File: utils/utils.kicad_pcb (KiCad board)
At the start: 2 copper layers, 34.8 x 70.5 mm, 37 parts, among them J1 A_IN, J2 B_IN, J3 GATE, J4 EURORACK_CONN_10, J5 ~OUT, J6 OUT, J7 Conn_01x04, J8 Conn_01x05, J9 Conn_01x03_Male, Q1 2N3904, U1 TL072, U2 4066, U3 LM317L_TO92, U4 LM337L_TO92

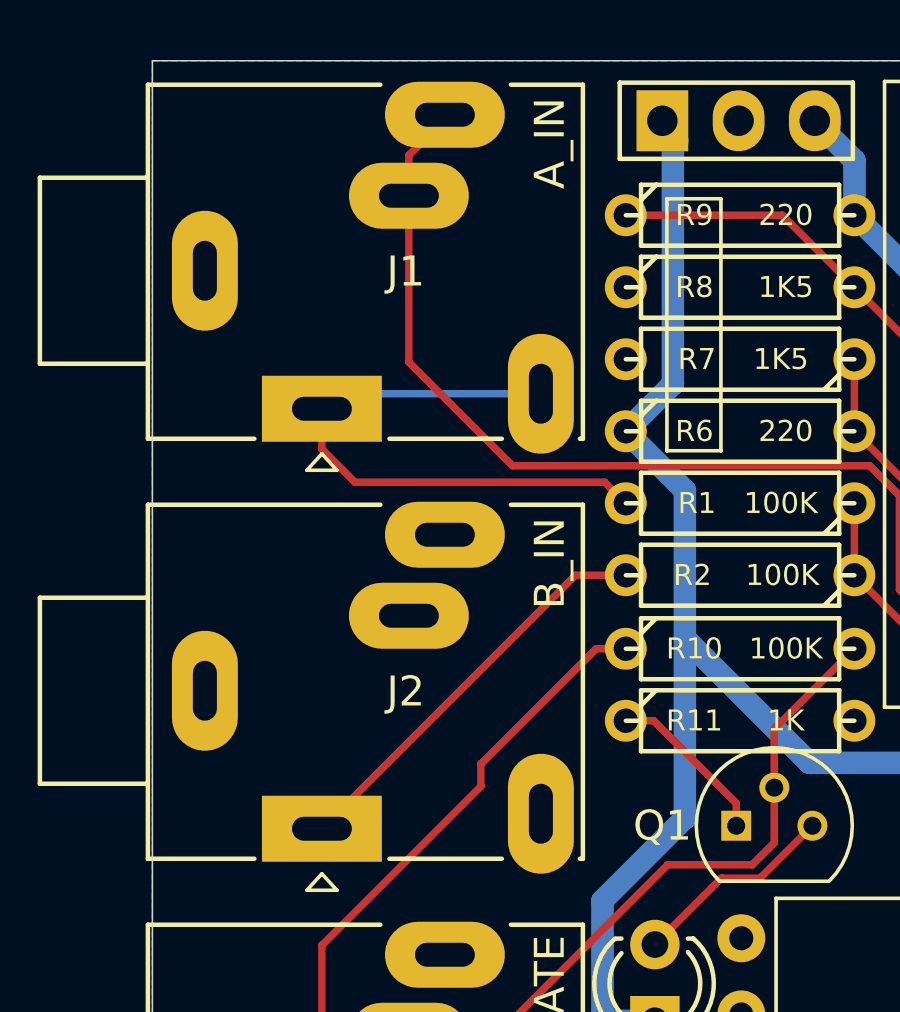
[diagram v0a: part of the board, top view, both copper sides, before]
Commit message: correct ground issue
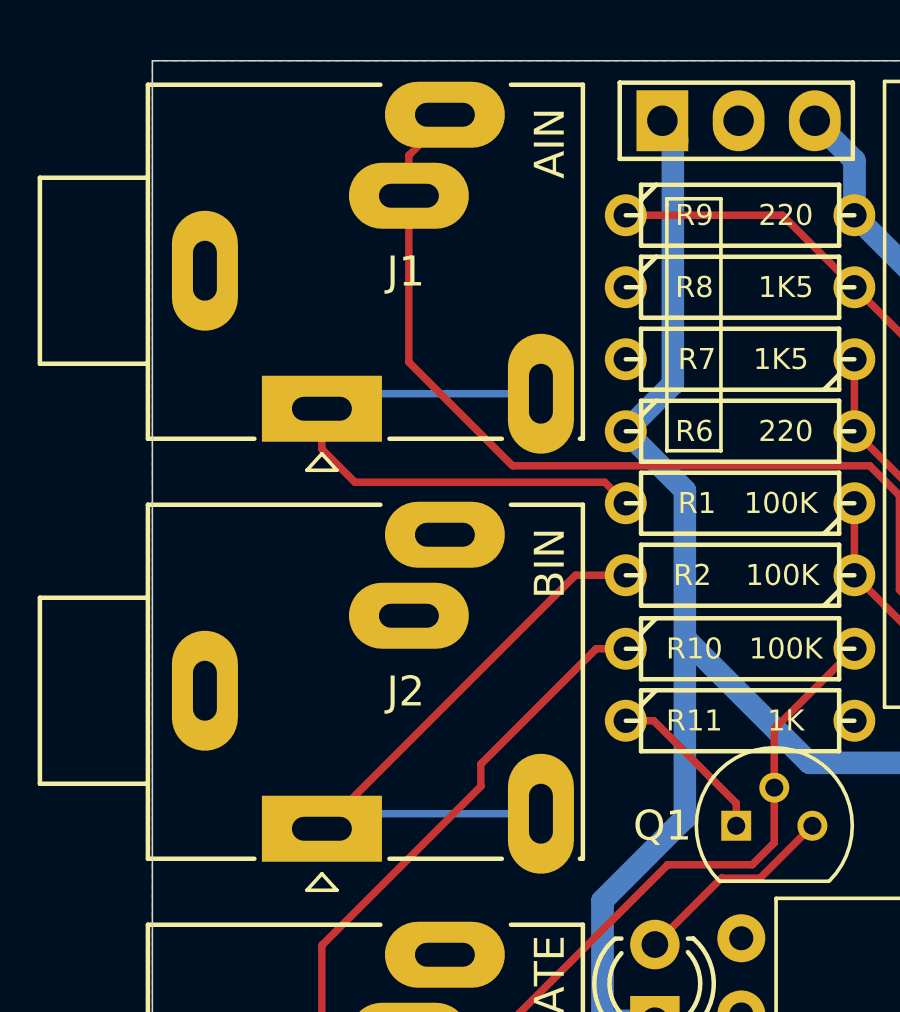
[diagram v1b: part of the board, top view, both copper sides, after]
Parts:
- J1: value A_IN -> AIN
- J2: value B_IN -> BIN
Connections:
- J2 pad TN: GND -> BIN
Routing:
- net BIN: track 13.6 -> 21.1 mm
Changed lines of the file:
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@@
     (thickness 1.6)
     (drawings 14)
-    (tracks 269)
+    (tracks 271)
     (zones 0)
     (modules 37)
@@
       (effects (font (size 1 1) (thickness 0.15)))
     )
-    (fp_text value A_IN (at 7.6 -8.85 90) (layer F.SilkS)
+    (fp_text value AIN (at 7.6 -8.85 90) (layer F.SilkS)
       (effects (font (size 1 1) (thickness 0.15)))
     )
@@
       (effects (font (size 1 1) (thickness 0.15)))
     )
-    (fp_text value B_IN (at 7.6 -8.85 270) (layer F.SilkS)
+    (fp_text value BIN (at 7.6 -8.85 270) (layer F.SilkS)
       (effects (font (size 1 1) (thickness 0.15)))
     )
@@
       (net 3 BIN))
     (pad TN thru_hole oval (at 7.3 -0.5 90) (size 4 2.2) (drill oval 2 0.8) (layers *.Cu *.Mask)
-      (net 1 GND))
+      (net 3 BIN))
     (pad SN thru_hole oval (at 2.9 -7.1) (size 4 2.2) (drill oval 2 0.8) (layers *.Cu *.Mask)
       (net 1 GND))
@@
   (segment (start 137.35 60.15) (end 128.9 68.6) (width 0.25) (layer F.Cu) (net 3))
   (segment (start 139.03 60.15) (end 137.35 60.15) (width 0.25) (layer F.Cu) (net 3))
+  (segment (start 129.4 68.1) (end 128.9 68.6) (width 0.25) (layer B.Cu) (net 3))
+  (segment (start 136.2 68.1) (end 129.4 68.1) (width 0.25) (layer B.Cu) (net 3))
   (segment (start 151.516 98.1) (end 151.192 98.424) (width 0.25) (layer F.Cu) (net 4))
   (segment (start 154.5 98.1) (end 151.516 98.1) (width 0.25) (layer F.Cu) (net 4))

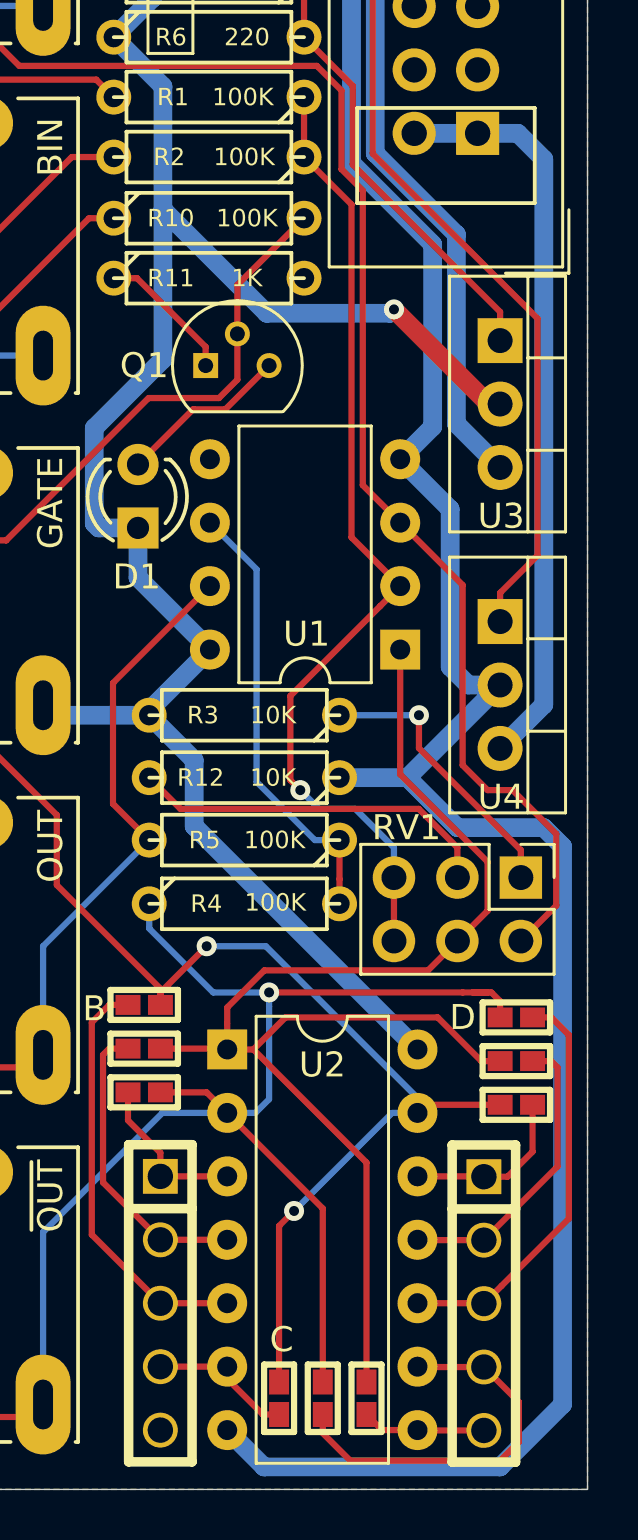
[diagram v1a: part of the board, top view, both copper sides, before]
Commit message: fix some bugs in the circuit
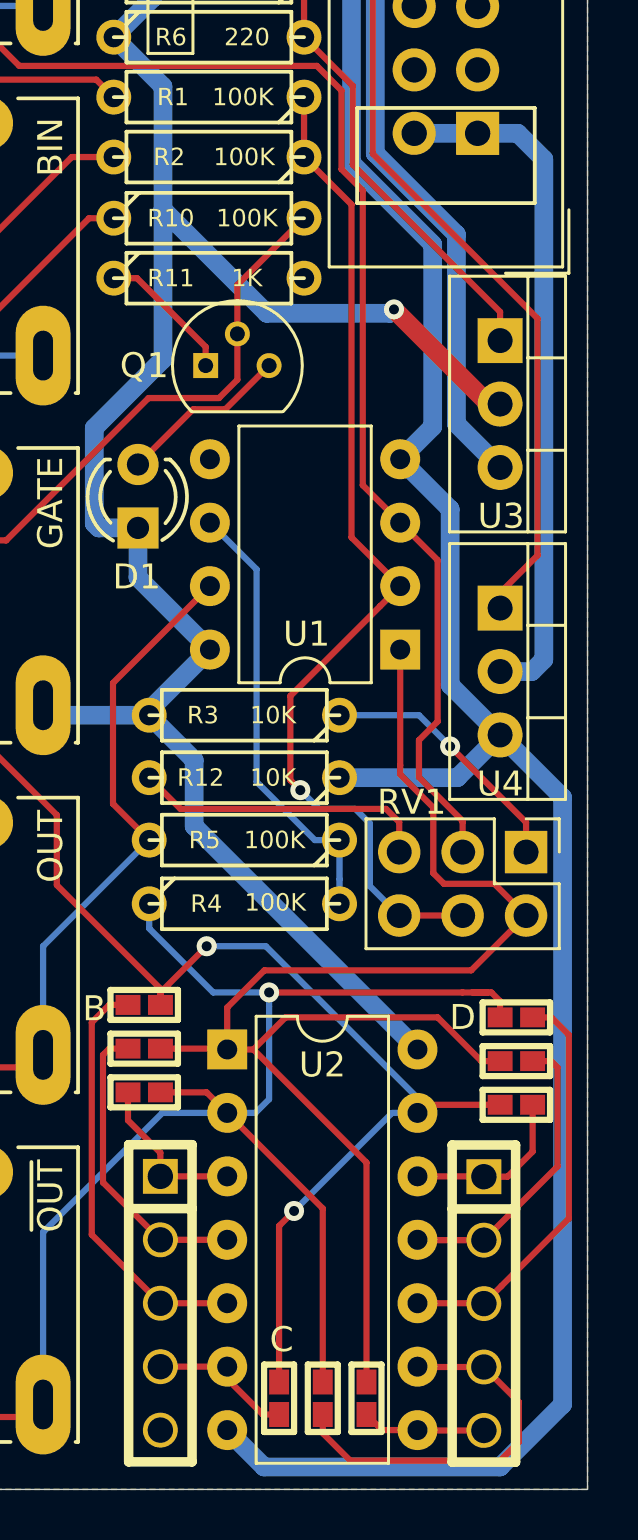
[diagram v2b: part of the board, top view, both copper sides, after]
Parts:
- U3: value LM317L_TO92 -> LM317
- U4: value LM337L_TO92 -> LM337
- moved RV1 1.04 mm to (153.0, 89.2)
- moved U4 0.54 mm to (154.5, 78.2)
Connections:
- U4 pad 2: -10V -> Net-(J4-Pad1)
- U4 pad 3: Net-(J4-Pad1) -> -10V
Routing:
- net A_CONN: track 65.7 -> 60.1 mm
- net STAGE1_OUT: track 55.7 -> 59.2 mm
- net Net-(R12-Pad2): track 14.7 -> 11.9 mm
- net Net-(J4-Pad1): track 29.9 -> 27.6 mm
- net -10V: track 95.2 -> 93.2 mm
- net Net-(R1-Pad1): track 40.0 -> 41.4 mm
- net Net-(R3-Pad1): track 11.4 -> 10.4 mm

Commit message: reworked utilities around better analog switch modules
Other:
- board text added: "TODO: this connector is backwards"

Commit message: restarted pcb
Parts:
- removed J1: AIN, synth:Jack_3.5mm_Ledino_KB3SPRS_Horizontal
- removed J2: BIN, synth:Jack_3.5mm_Ledino_KB3SPRS_Horizontal
- removed J3: GATE, synth:Jack_3.5mm_Ledino_KB3SPRS_Horizontal
- removed J4: EURORACK_CONN_10, synth:EURORACK_10_IDC
- removed J5: ~OUT, synth:Jack_3.5mm_Ledino_KB3SPRS_Horizontal
- removed J7: Conn_01x04, imciner2/KiCad-Libraries/modules/Connectors.pretty:CONN_2.54mm_1x05
- removed J8: Conn_01x05, imciner2/KiCad-Libraries/modules/Connectors.pretty:CONN_2.54mm_1x05
- removed J9: Conn_01x03_Male, 4ms/4ms-kicad-lib/4ms-footprints.pretty:Pin_Header_Straight_1x03
- removed JP1, JP2, JP3, JP4, JP5, JP6, JP7, JP8, JP9: Jumper_2_Open, fruchti/fruchtilib/mod/rcl.pretty:SOLDER_JUMPER_0603_B
- removed R10: 100K, 4ms/4ms-kicad-lib/4ms-footprints.pretty:Resistor_TH_300
- removed R11: 1K, 4ms/4ms-kicad-lib/4ms-footprints.pretty:Resistor_TH_300
- removed R12: 10K, 4ms/4ms-kicad-lib/4ms-footprints.pretty:Resistor_TH_300
- removed U3: LM317, KiCad/TO_SOT_Packages_THT.pretty:TO-220-3_Vertical
- removed U4: LM337, KiCad/TO_SOT_Packages_THT.pretty:TO-220-3_Vertical
- added A_IN1: AudioJack2_Ground_Switch, synth:Jack_3.5mm_Ledino_KB3SPRS_Horizontal, F.Cu at (125.5, 50.0)
- added B_IN1: AudioJack2_Ground_Switch, synth:Jack_3.5mm_Ledino_KB3SPRS_Horizontal, F.Cu at (125.5, 64.0)
- added GATE1: AudioJack2_Ground_Switch, synth:Jack_3.5mm_Ledino_KB3SPRS_Horizontal, F.Cu at (125.5, 78.0)
- added OUT1: AudioJack2_Ground_Switch, synth:Jack_3.5mm_Ledino_KB3SPRS_Horizontal, F.Cu at (125.5, 92.0)
- added Q2: 2N3904, Package_TO_SOT_THT:TO-92, F.Cu at (141.5, 53.5)
- added Q3: 2N3904, Package_TO_SOT_THT:TO-92, F.Cu at (141.0, 61.0)
- added ~OUT1: AudioJack2_Ground_Switch, synth:Jack_3.5mm_Ledino_KB3SPRS_Horizontal, F.Cu at (125.5, 106.0)
- J6: value OUT -> EURORACK_CONN_16; footprint synth:Jack_3.5mm_Ledino_KB3SPRS_Horizontal -> synth:EURORACK_16_IDC
- Q1: footprint 4ms/4ms-kicad-lib/lib-footprints/4ms_Package_TO.pretty:TO-92_OffsetPin2 -> Package_TO_SOT_THT:TO-92
- R1, R2, R4, R5: footprint 4ms/4ms-kicad-lib/4ms-footprints.pretty:Resistor_TH_300 -> Resistor_THT:R_Axial_DIN0309_L9.0mm_D3.2mm_P2.54mm_Vertical
- R3: value 10K -> 100K; footprint 4ms/4ms-kicad-lib/4ms-footprints.pretty:Resistor_TH_300 -> Resistor_THT:R_Axial_DIN0309_L9.0mm_D3.2mm_P2.54mm_Vertical
- R6, R9: value 220 -> 100K; footprint 4ms/4ms-kicad-lib/4ms-footprints.pretty:Resistor_TH_300 -> Resistor_THT:R_Axial_DIN0309_L9.0mm_D3.2mm_P2.54mm_Vertical
- R7: value 1K5 -> 100K; footprint 4ms/4ms-kicad-lib/4ms-footprints.pretty:Resistor_TH_300 -> Resistor_THT:R_Axial_DIN0309_L9.0mm_D3.2mm_P2.54mm_Vertical
- R8: value 1K5 -> 1K; footprint 4ms/4ms-kicad-lib/4ms-footprints.pretty:Resistor_TH_300 -> Resistor_THT:R_Axial_DIN0309_L9.0mm_D3.2mm_P2.54mm_Vertical
- RV1: footprint 4ms/4ms-kicad-lib/4ms-footprints.pretty:Pin_Header_Straight_2x03_Pitch2.54mm -> Connector_PinHeader_2.54mm:PinHeader_2x03_P2.54mm_Vertical
- U1: value TL072 -> TL074; footprint KiCad/kicad-footprints/Package_DIP.pretty:DIP-8_W7.62mm -> Package_DIP:DIP-14_W7.62mm
- U2: value 4066 -> DG403; footprint KiCad/kicad-footprints/Package_DIP.pretty:DIP-14_W7.62mm -> Package_SO:SOIC-16_3.9x9.9mm_P1.27mm
- moved R6 54.4 mm to (170.8, 102.0)
- moved R9 51.5 mm to (166.2, 94.0)
- moved J6 39.5 mm to (154.3, 66.3), turned to 180 degrees
- moved R5 36.0 mm to (146.0, 51.5), turned to 270 degrees
- moved U1 31.4 mm to (151.5, 111.2)
- moved R4 23.1 mm to (141.0, 67.2), turned to 270 degrees
- moved Q1 21.4 mm to (141.5, 47.2), turned to 90 degrees
- moved R3 19.4 mm to (146.2, 63.2), turned to 90 degrees
- moved R1 17.8 mm to (145.8, 75.3), turned to 90 degrees
- moved R7 16.6 mm to (146.0, 69.3), turned to 90 degrees
- moved R2 15.2 mm to (146.0, 45.2), turned to 270 degrees
- moved U2 7.88 mm to (143.5, 88.0)
- moved R8 7.03 mm to (140.7, 57.2)
- moved RV1 2.37 mm to (155.2, 90.0), turned to 180 degrees
- moved D1 0.90 mm to (140.8, 74.2)
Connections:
- D1 pad 2: +10V -> +5V
- Q1 pad 1: Net-(Q1-Pad1) -> GND
- Q1 pad 2: GATE_CONN -> A_CONN
- Q1 pad 3: Net-(D1-Pad1) -> CONST
- R1 pad 1: Net-(R1-Pad1) -> +5V
- R1 pad 2: AIN -> A_CONN
- R2 pad 1: Net-(R1-Pad1) -> +5V
- R2 pad 2: BIN -> CONST
- R3 pad 2: +10V -> AIN
- R4 pad 1: ~OUT -> Net-(R3-Pad1)
- R4 pad 2: Net-(R4-Pad2) -> BIN
- R5 pad 1: Net-(R4-Pad2) -> +5V
- R5 pad 2: OUT -> B_CONN
- R6 pad 1: +10V -> Net-(R6-Pad1)
- R7 pad 1: Net-(R6-Pad2) -> GATE
- R7 pad 2: GND -> GATE_CONN
- R8 pad 1: GND -> Net-(Q3-Pad1)
- R8 pad 2: Net-(R8-Pad2) -> GND
- R9 pad 1: Net-(R8-Pad2) -> Net-(R6-Pad2)
- R9 pad 2: -10V -> OUT
- RV1 pad 1: Net-(R3-Pad1) -> +12V
- RV1 pad 2: A_CONN -> Net-(RV1-Pad2)
- RV1 pad 3: Net-(R12-Pad2) -> -12V
- RV1 pad 4: STAGE1_OUT -> Net-(RV1-Pad4)
- RV1 pad 5: Net-(R1-Pad1) -> Net-(R3-Pad1)
- RV1 pad 6: Net-(R1-Pad1) -> Net-(R3-Pad1)
- U1 pad 1: STAGE1_OUT -> Net-(U1-Pad1)
- U1 pad 2: Net-(R1-Pad1) -> Net-(U1-Pad1)
- U1 pad 3: A_CONN -> Net-(RV1-Pad2)
- U1 pad 4: -10V -> +12V
- U1 pad 6: Net-(R4-Pad2) -> Net-(R3-Pad1)
- U1 pad 7: OUT -> Net-(RV1-Pad4)
- U1 pad 8: +10V -> OUT
- U2 pad 1: STAGE1_OUT -> Net-(U1-Pad1)
- U2 pad 10: 4066_10 -> GATE
- U2 pad 11: 4066_11 -> +12V
- U2 pad 12: 4066_12 -> +5V
- U2 pad 13: GATE -> GND
- U2 pad 14: +10V -> -12V
- U2 pad 2: ~OUT -> Net-(U2-Pad2)
- U2 pad 3: 4066_3 -> Net-(RV1-Pad4)
- U2 pad 4: 4066_4 -> Net-(U2-Pad16)
- U2 pad 5: 4066_5 -> Net-(R6-Pad1)
- U2 pad 6: 4066_6 -> GND
- U2 pad 7: -10V -> Net-(U2-Pad7)
- U2 pad 8: 4066_8 -> Net-(U2-Pad16)
- U2 pad 9: 4066_9 -> Net-(R6-Pad1)
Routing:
- net -10V: track 93.2 -> 0.00 mm
- net +10V: track 84.8 -> 0.00 mm, vias 1 -> 0
- net GATE: track 74.8 -> 0.00 mm, vias 2 -> 0
- net ~OUT: track 62.8 -> 0.00 mm, vias 1 -> 0
- net A_CONN: track 60.1 -> 0.00 mm
- net STAGE1_OUT: track 59.2 -> 0.00 mm
- net Net-(R1-Pad1): track 41.4 -> 0.00 mm, vias 1 -> 0
- net Net-(R8-Pad2): track 41.3 -> 0.00 mm
- net OUT: track 30.2 -> 0.00 mm
- net Net-(J4-Pad9): track 28.8 -> 0.00 mm
- net Net-(J4-Pad1): track 27.6 -> 0.00 mm
- net GATE_CONN: track 22.4 -> 0.00 mm
- net BIN: track 21.1 -> 0.00 mm
- net AIN: track 19.7 -> 0.00 mm
- net Net-(R4-Pad2): track 18.0 -> 0.00 mm
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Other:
- board text removed: "B"
- board text removed: "C"
- board text removed: "D"
- board text removed: "TODO: this connector is backwards"

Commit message: rework PCB
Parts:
- R1, R3, R8: footprint Resistor_THT:R_Axial_DIN0309_L9.0mm_D3.2mm_P2.54mm_Vertical -> Resistor_THT:R_Axial_DIN0204_L3.6mm_D1.6mm_P5.08mm_Horizontal
- moved R6 29.7 mm to (141.2, 98.3), turned to 90 degrees
- moved R9 25.1 mm to (141.2, 92.3), turned to 90 degrees
- moved R1 18.0 mm to (146.0, 57.2), turned to 180 degrees
- moved RV1 16.1 mm to (152.2, 74.2), turned to 0 degrees
- moved R8 8.00 mm to (146.0, 63.2), turned to 180 degrees
- moved Q3 7.18 mm to (145.2, 66.8)
- moved U1 6.02 mm to (153.1, 105.5)
- moved R7 5.47 mm to (145.8, 74.8)
- moved U2 4.50 mm to (144.0, 83.5), turned to 90 degrees
- moved R3 3.00 mm to (146.1, 60.2), turned to 180 degrees
- moved R4 0.52 mm to (140.8, 66.8)
- moved D1 0.50 mm to (140.8, 73.7)
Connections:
- U2 pad 1: Net-(U1-Pad1) -> Net-(U2-Pad1)
- U2 pad 10: GATE -> CONST
- U2 pad 15: CONST -> GATE
- U2 pad 16: Net-(U2-Pad16) -> Net-(R6-Pad1)
- U2 pad 3: Net-(RV1-Pad4) -> GND
- U2 pad 4: Net-(U2-Pad16) -> Net-(R6-Pad1)
- U2 pad 5: Net-(R6-Pad1) -> Net-(U2-Pad1)
- U2 pad 6: GND -> Net-(RV1-Pad4)
- U2 pad 8: Net-(U2-Pad16) -> Net-(U1-Pad1)
- U2 pad 9: Net-(R6-Pad1) -> Net-(U2-Pad1)
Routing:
- net +12V: track 0.00 -> 70.4 mm, vias 0 -> 1
- net +5V: track 0.00 -> 64.3 mm, vias 0 -> 1
- net -12V: track 0.00 -> 50.6 mm, vias 0 -> 1
- net Net-(R3-Pad1): track 0.00 -> 48.1 mm, vias 0 -> 1
- net CONST: track 0.00 -> 45.4 mm
- net Net-(R6-Pad1): track 0.00 -> 31.3 mm
- net Net-(RV1-Pad2): track 0.00 -> 28.7 mm
- net Net-(RV1-Pad4): track 0.00 -> 27.1 mm, vias 0 -> 1
- net GATE: track 0.00 -> 24.1 mm
- net A_CONN: track 0.00 -> 23.2 mm
- net ~OUT: track 0.00 -> 21.9 mm
- net Net-(U1-Pad1): track 0.00 -> 21.4 mm
- net GATE_CONN: track 0.00 -> 20.7 mm
- net OUT: track 0.00 -> 20.5 mm
- net B_CONN: track 0.00 -> 20.3 mm
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
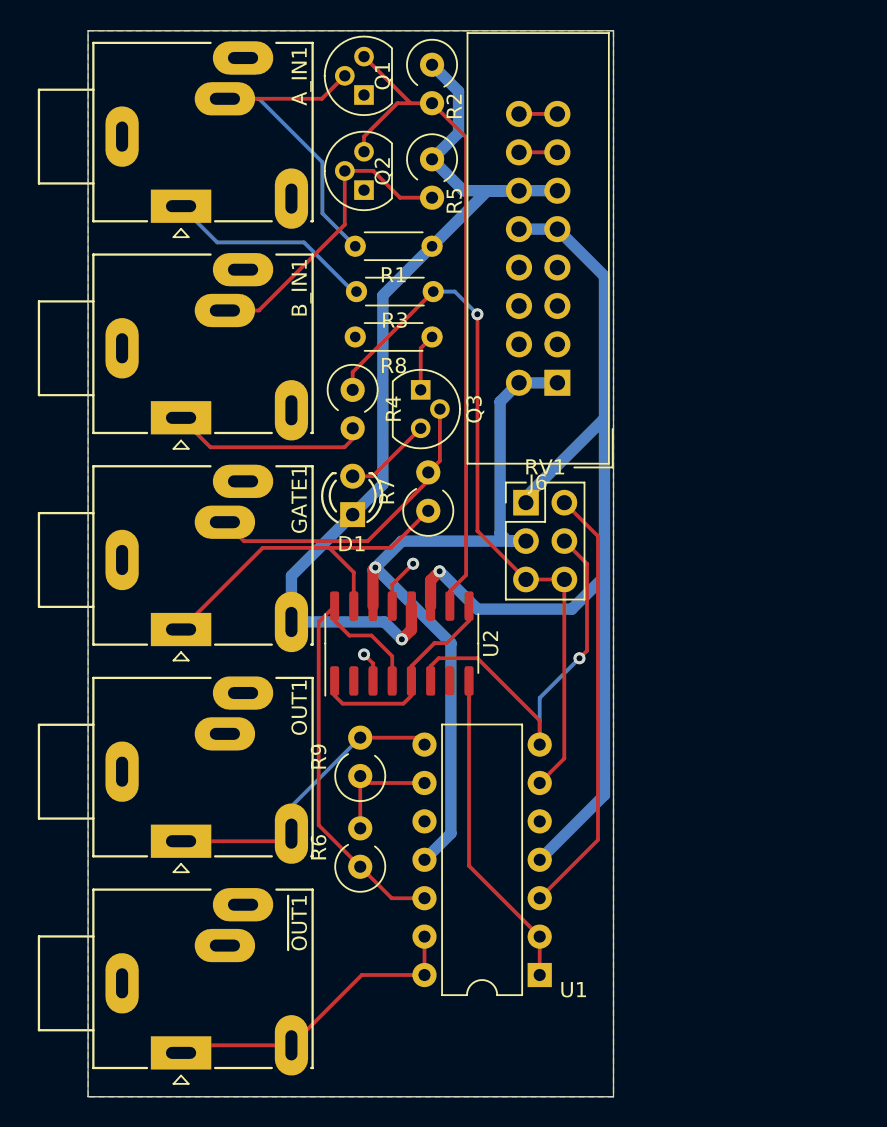
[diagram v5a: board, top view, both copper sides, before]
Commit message: reworked silkscreen
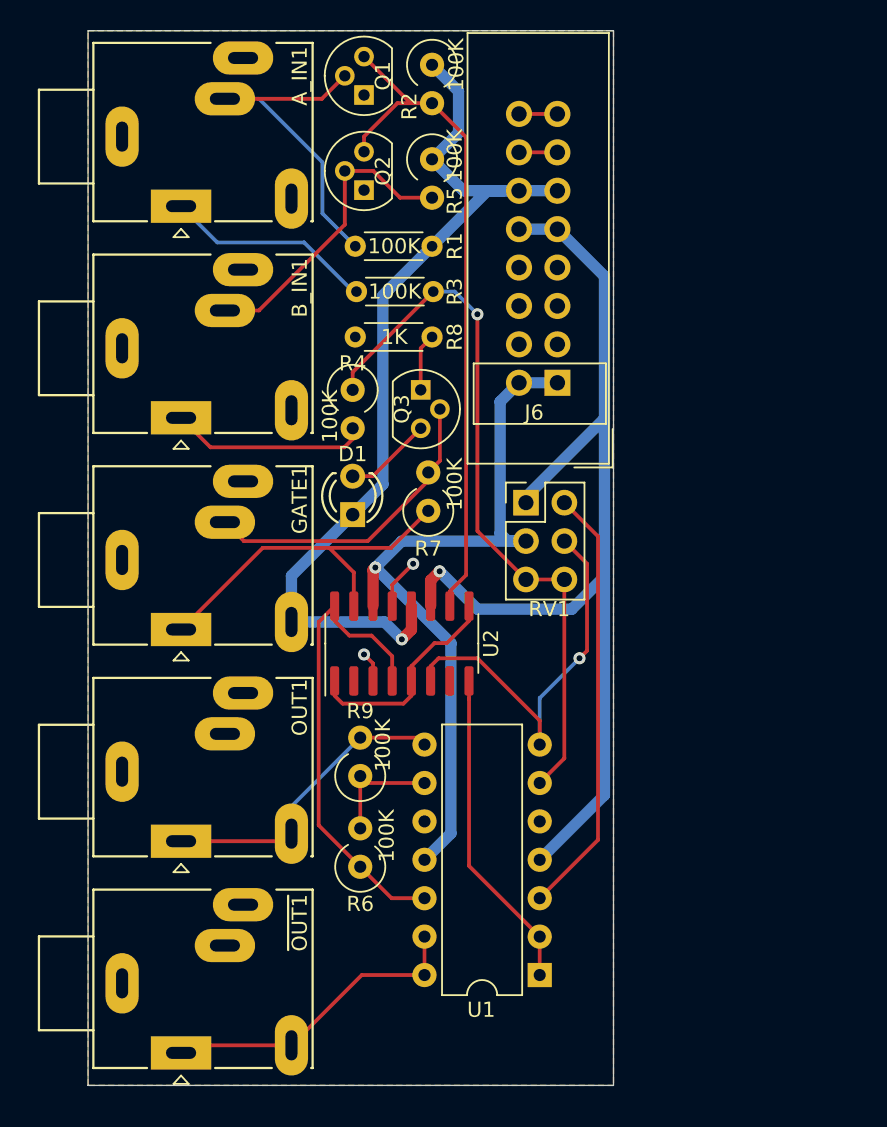
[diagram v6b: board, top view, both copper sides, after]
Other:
- board size 34.8 x 70.5 mm -> 34.8 x 69.8 mm
- board text added: "Rev. B | 2020-07-04"
- board text removed: "Rev. A | 2020-05-23"
